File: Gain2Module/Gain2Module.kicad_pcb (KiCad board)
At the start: 2 copper layers, 56 x 60 mm, 19 parts, among them J1 SigIn, J2 SigOut, J3 Heater, J4 HeaterOut, J5 HV, J6 HVOut, U1 ECC83

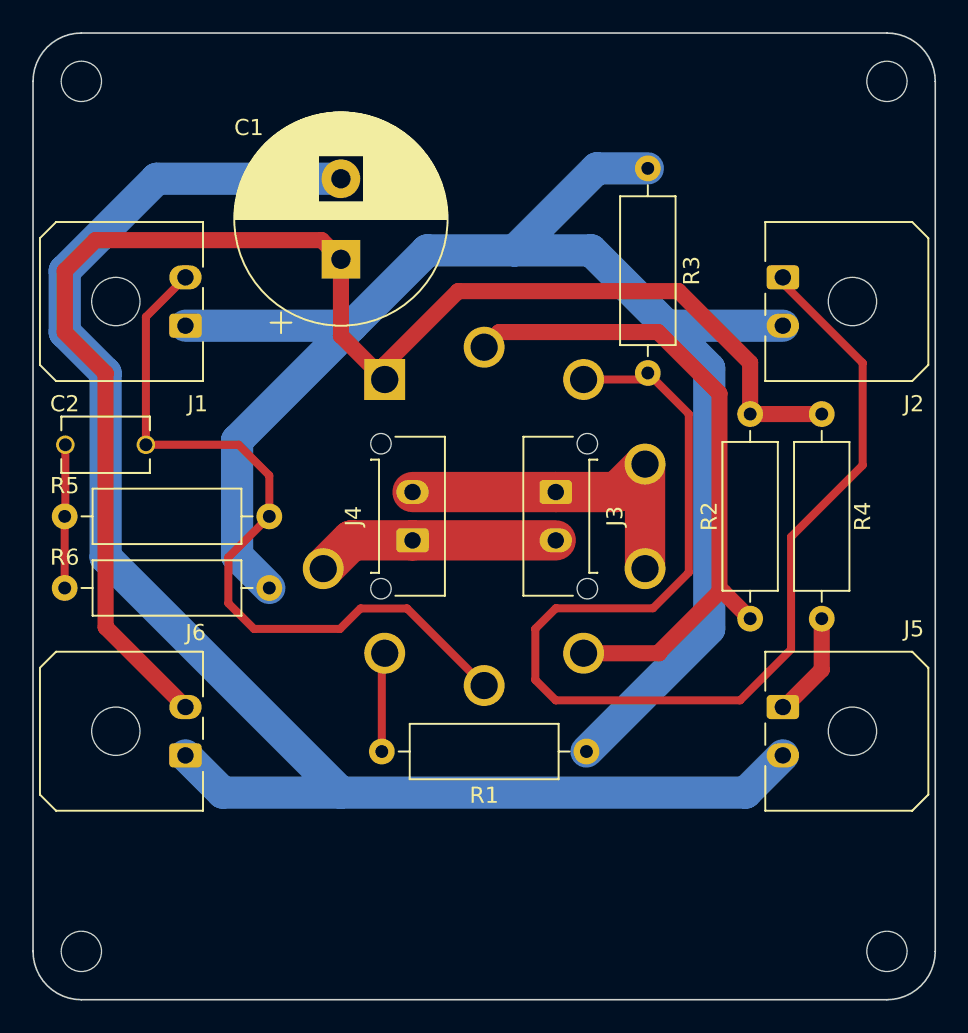
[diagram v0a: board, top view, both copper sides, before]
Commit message: Change connector footprints to contain 3D models. Make necessary PCB modifications to address errors found in the design
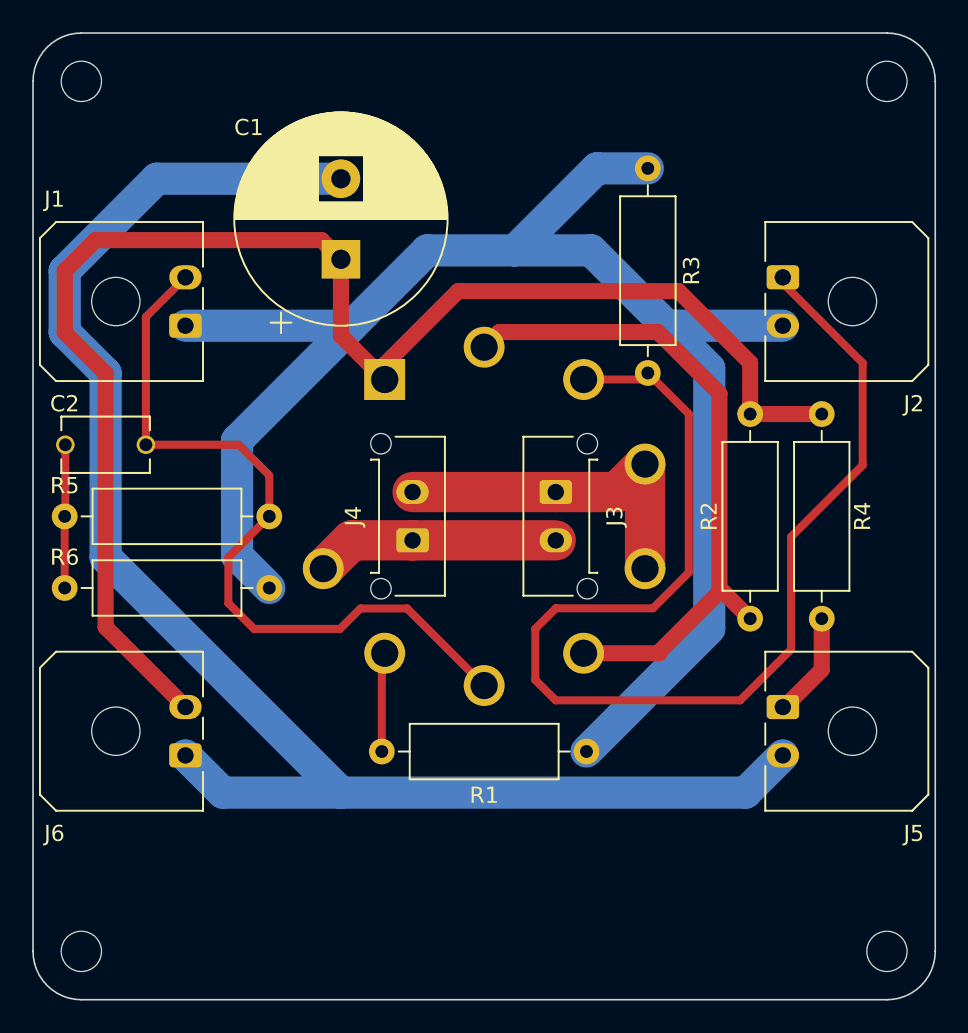
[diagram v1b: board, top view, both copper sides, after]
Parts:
- J1, J2, J5, J6: footprint Connector_Molex:Molex_Micro-Fit_3.0_43650-0200_1x02_P3.00mm_Horizontal -> CustomFootprints:Molex_Micro-Fit_3.0_43650-0200_1x02_P3.00mm_Horizontal
- J3, J4: footprint Connector_Molex:Molex_Micro-Fit_3.0_43650-0215_1x02_P3.00mm_Vertical -> CustomFootprints:Molex_Micro-Fit_3.0_43650-0215_1x02_P3.00mm_Vertical
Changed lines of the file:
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@@
     )
   )
-  (footprint "Connector_Molex:Molex_Micro-Fit_3.0_43650-0215_1x02_P3.00mm_Vertical" (layer "F.Cu")
+  (footprint "CustomFootprints:Molex_Micro-Fit_3.0_43650-0215_1x02_P3.00mm_Vertical" (layer "F.Cu")
     (at 128.905 98.02 90)
     (descr "Molex Micro-Fit 3.0 Connector System, 43650-0215 (compatible alternatives: 43650-0216, 43650-0217), 2 Pins per row (http://www.molex.com/pdm_docs/sd/436500215_sd.pdf), generated with kicad-footprint-generator")
@@
         (effects (font (size 1 1) (thickness 0.15)))
     )
-    (fp_text value "HeaterOut" (at -4.215 0 180) (layer "F.Fab")
+    (fp_text value "HeaterOut" (at 1.5 4.5 90) (layer "F.Fab")
         (effects (font (size 1 1) (thickness 0.15)))
     )
@@
       (rotate (xyz 0 0 0))
     )
+    (model "C:/Users/dillo/Downloads/436500215_stp/436500215.stp"
+      (offset (xyz 1.5 1.9 10))
+      (scale (xyz 1 1 1))
+      (rotate (xyz 90 0 180))
+    )
   )
   (footprint "Resistor_THT:R_Axial_DIN0309_L9.0mm_D3.2mm_P12.70mm_Horizontal" (layer "F.Cu")
@@
     (pad "" np_thru_hole circle (at 0 0) (size 2.5 2.5) (drill 2.5) (layers "F&B.Cu" "*.Mask"))
   )
-  (footprint "Connector_Molex:Molex_Micro-Fit_3.0_43650-0200_1x02_P3.00mm_Horizontal" (layer "F.Cu")
+  (footprint "CustomFootprints:Molex_Micro-Fit_3.0_43650-0200_1x02_P3.00mm_Horizontal" (layer "F.Cu")
     (at 151.89 108.365 -90)
     (descr "Molex Micro-Fit 3.0 Connector System, 43650-0200 (compatible alternatives: 43650-0201, 43650-0202), 2 Pins per row (https://www.molex.com/pdm_docs/sd/436500300_sd.pdf), generated with kicad-footprint-generator")
@@
     (property "ki_keywords" "screw terminal")
     (attr through_hole)
-    (fp_text reference "J5" (at -4.85 -8.13 -180) (layer "F.SilkS")
-        (effects (font (size 1 1) (thickness 0.15)))
-    )
-    (fp_text value "HV" (at 1.5 -6.86 90) (layer "F.Fab")
-        (effects (font (size 1 1) (thickness 0.15)))
-    )
-    (fp_text user "${REFERENCE}" (at 1.5 -8.22 90) (layer "F.Fab")
+    (fp_text reference "J5" (at 7.85 -8.13) (layer "F.SilkS")
+        (effects (font (size 1 1) (thickness 0.15)))
+    )
+    (fp_text value "HV" (at 1.5 3.22 -90) (layer "F.Fab")
+        (effects (font (size 1 1) (thickness 0.15)))
+    )
+    (fp_text user "${REFERENCE}" (at 1.5 -8.22 -90) (layer "F.Fab")
         (effects (font (size 1 1) (thickness 0.15)))
     )
@@
       (rotate (xyz 0 0 0))
     )
+    (model "C:/Users/dillo/Downloads/436500200_stp/436500200.stp"
+      (offset (xyz 1.5 8.9 0.5))
+      (scale (xyz 1 1 1))
+      (rotate (xyz 0 0 180))
+    )
   )
   (footprint "Resistor_THT:R_Axial_DIN0309_L9.0mm_D3.2mm_P12.70mm_Horizontal" (layer "F.Cu")
@@
     )
   )
-  (footprint "Connector_Molex:Molex_Micro-Fit_3.0_43650-0200_1x02_P3.00mm_Horizontal" (layer "F.Cu")
+  (footprint "CustomFootprints:Molex_Micro-Fit_3.0_43650-0200_1x02_P3.00mm_Horizontal" (layer "F.Cu")
     (at 114.81 111.365 90)
     (descr "Molex Micro-Fit 3.0 Connector System, 43650-0200 (compatible alternatives: 43650-0201, 43650-0202), 2 Pins per row (https://www.molex.com/pdm_docs/sd/436500300_sd.pdf), generated with kicad-footprint-generator")
@@
     (property "ki_keywords" "screw terminal")
     (attr through_hole)
-    (fp_text reference "J6" (at 7.62 0.635 180) (layer "F.SilkS")
-        (effects (font (size 1 1) (thickness 0.15)))
-    )
-    (fp_text value "HVOut" (at 1.5 -6.985 90) (layer "F.Fab")
+    (fp_text reference "J6" (at -4.85 -8.13 180) (layer "F.SilkS")
+        (effects (font (size 1 1) (thickness 0.15)))
+    )
+    (fp_text value "HVOut" (at 1.5 3.22 90) (layer "F.Fab")
         (effects (font (size 1 1) (thickness 0.15)))
     )
@@
       (rotate (xyz 0 0 0))
     )
+    (model "C:/Users/dillo/Downloads/436500200_stp/436500200.stp"
+      (offset (xyz 1.5 8.9 0.5))
+      (scale (xyz 1 1 1))
+      (rotate (xyz 0 0 180))
+    )
   )
   (footprint "MountingHole:MountingHole_2.5mm" (layer "F.Cu")
@@
     (pad "" np_thru_hole circle (at 0 0) (size 2.5 2.5) (drill 2.5) (layers "F&B.Cu" "*.Mask"))
   )
-  (footprint "Connector_Molex:Molex_Micro-Fit_3.0_43650-0200_1x02_P3.00mm_Horizontal" (layer "F.Cu")
+  (footprint "CustomFootprints:Molex_Micro-Fit_3.0_43650-0200_1x02_P3.00mm_Horizontal" (layer "F.Cu")
     (at 114.81 84.695 90)
     (descr "Molex Micro-Fit 3.0 Connector System, 43650-0200 (compatible alternatives: 43650-0201, 43650-0202), 2 Pins per row (https://www.molex.com/pdm_docs/sd/436500300_sd.pdf), generated with kicad-footprint-generator")
@@
     (property "ki_keywords" "screw terminal")
     (attr through_hole)
-    (fp_text reference "J1" (at -4.85 0.76 180) (layer "F.SilkS")
-        (effects (font (size 1 1) (thickness 0.15)))
-    )
-    (fp_text value "SigIn" (at 1.5 -7.495 90) (layer "F.Fab")
+    (fp_text reference "J1" (at 7.85 -8.13 180) (layer "F.SilkS")
+        (effects (font (size 1 1) (thickness 0.15)))
+    )
+    (fp_text value "SigIn" (at 1.5 3.22 90) (layer "F.Fab")
         (effects (font (size 1 1) (thickness 0.15)))
     )
@@
       (scale (xyz 1 1 1))
       (rotate (xyz 0 0 0))
+    )
+    (model "C:/Users/dillo/Downloads/436500200_stp/436500200.stp"
+      (offset (xyz 1.5 8.9 0.5))
+      (scale (xyz 1 1 1))
+      (rotate (xyz 0 0 180))
     )
   )
@@
     )
   )
-  (footprint "Connector_Molex:Molex_Micro-Fit_3.0_43650-0200_1x02_P3.00mm_Horizontal" (layer "F.Cu")
+  (footprint "CustomFootprints:Molex_Micro-Fit_3.0_43650-0200_1x02_P3.00mm_Horizontal" (layer "F.Cu")
     (at 151.89 81.695 -90)
     (descr "Molex Micro-Fit 3.0 Connector System, 43650-0200 (compatible alternatives: 43650-0201, 43650-0202), 2 Pins per row (https://www.molex.com/pdm_docs/sd/436500300_sd.pdf), generated with kicad-footprint-generator")
@@
     (property "ki_keywords" "screw terminal")
     (attr through_hole)
-    (fp_text reference "J2" (at 7.85 -8.13 -180) (layer "F.SilkS")
-        (effects (font (size 1 1) (thickness 0.15)))
-    )
-    (fp_text value "SigOut" (at 1.5 -6.86 90) (layer "F.Fab")
-        (effects (font (size 1 1) (thickness 0.15)))
-    )
-    (fp_text user "${REFERENCE}" (at 1.5 -8.22 90) (layer "F.Fab")
+    (fp_text reference "J2" (at 7.85 -8.13) (layer "F.SilkS")
+        (effects (font (size 1 1) (thickness 0.15)))
+    )
+    (fp_text value "SigOut" (at 1.5 3.22 -90) (layer "F.Fab")
+        (effects (font (size 1 1) (thickness 0.15)))
+    )
+    (fp_text user "${REFERENCE}" (at 1.5 -8.22 -90) (layer "F.Fab")
         (effects (font (size 1 1) (thickness 0.15)))
     )
@@
       (rotate (xyz 0 0 0))
     )
-  )
-  (footprint "Connector_Molex:Molex_Micro-Fit_3.0_43650-0215_1x02_P3.00mm_Vertical" (layer "F.Cu")
+    (model "C:/Users/dillo/Downloads/436500200_stp/436500200.stp"
+      (offset (xyz 1.5 8.9 0.5))
+      (scale (xyz 1 1 1))
+      (rotate (xyz 0 0 180))
+    )
+  )
+  (footprint "CustomFootprints:Molex_Micro-Fit_3.0_43650-0215_1x02_P3.00mm_Vertical" (layer "F.Cu")
     (at 137.795 95.02 -90)
     (descr "Molex Micro-Fit 3.0 Connector System, 43650-0215 (compatible alternatives: 43650-0216, 43650-0217), 2 Pins per row (http://www.molex.com/pdm_docs/sd/436500215_sd.pdf), generated with kicad-footprint-generator")
@@
     (property "ki_keywords" "screw terminal")
     (attr through_hole)
-    (fp_text reference "J3" (at 1.5 -3.67 90) (layer "F.SilkS")
-        (effects (font (size 1 1) (thickness 0.15)))
-    )
-    (fp_text value "Heater" (at 7.215 0 -180) (layer "F.Fab")
-        (effects (font (size 1 1) (thickness 0.15)))
-    )
-    (fp_text user "${REFERENCE}" (at 1.5 1.2 90) (layer "F.Fab")
+    (fp_text reference "J3" (at 1.5 -3.67 -90) (layer "F.SilkS")
+        (effects (font (size 1 1) (thickness 0.15)))
+    )
+    (fp_text value "Heater" (at 1.5 4.5 -90) (layer "F.Fab")
+        (effects (font (size 1 1) (thickness 0.15)))
+    )
+    (fp_text user "${REFERENCE}" (at 1.5 1.2 -90) (layer "F.Fab")
         (effects (font (size 1 1) (thickness 0.15)))
     )
@@
       (rotate (xyz 0 0 0))
     )
-  )
+    (model "C:/Users/dillo/Downloads/436500215_stp/436500215.stp"
+      (offset (xyz 1.5 1.9 10))
+      (scale (xyz 1 1 1))
+      (rotate (xyz 90 0 180))
+    )
+  )
